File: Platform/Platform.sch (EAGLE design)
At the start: 21 parts, among them IC1 5v

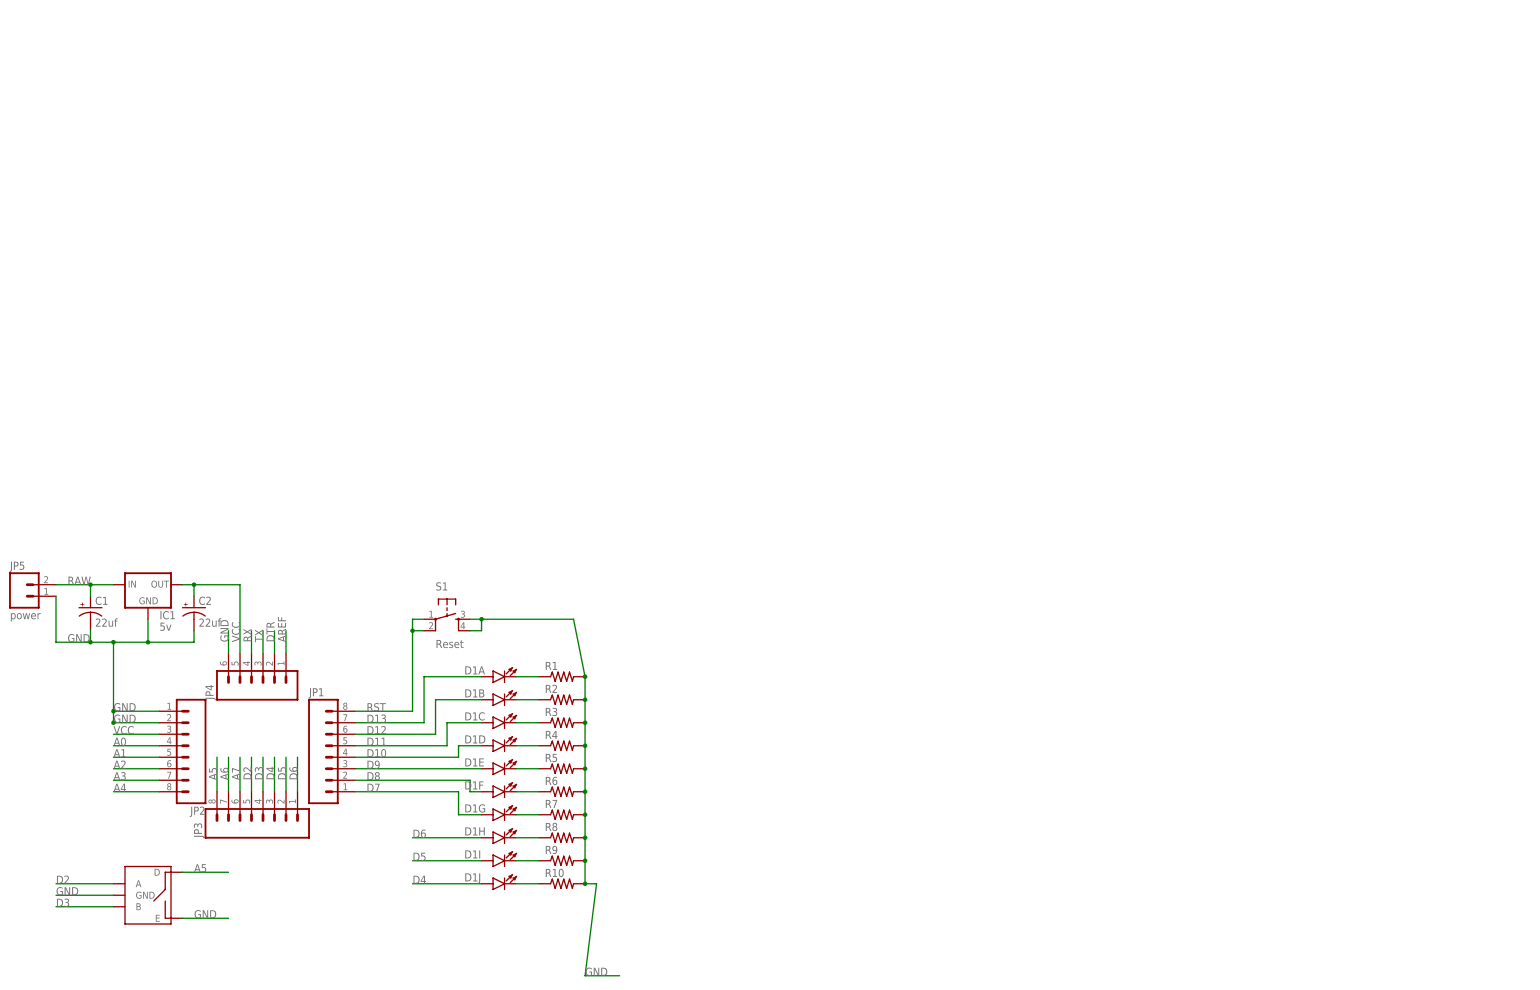
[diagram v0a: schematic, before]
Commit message: fixed up design rules. Copied the actual newest boards into t the project
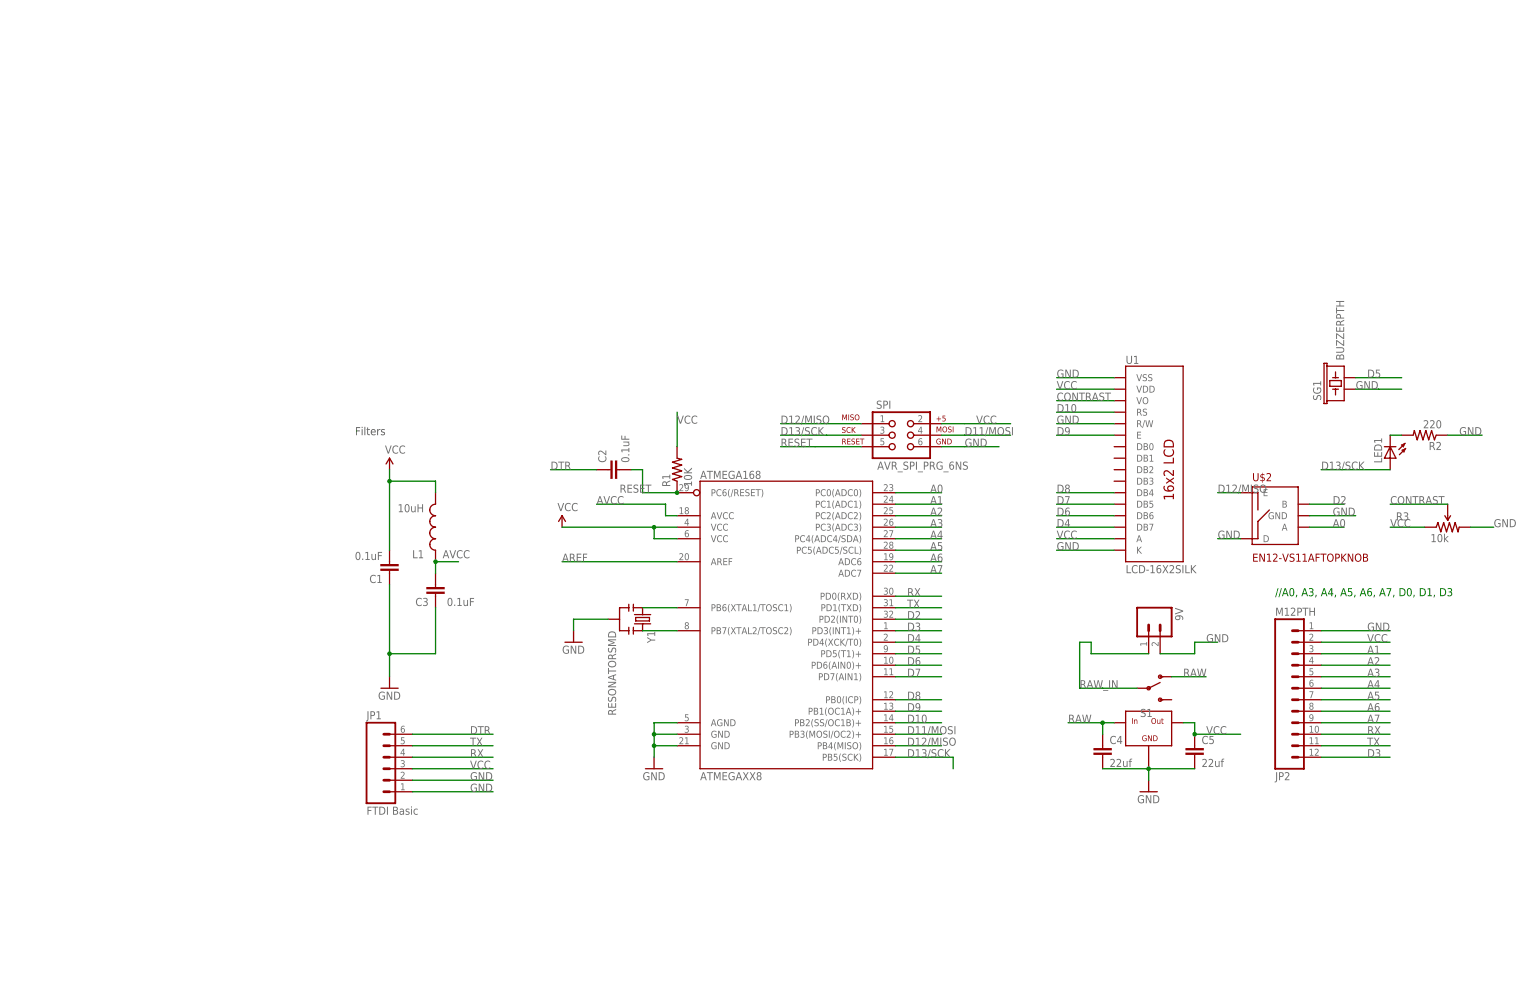
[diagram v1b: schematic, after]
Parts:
- removed D1: (no value), SparkFun:LED_BARGRAPH_10
- removed IC1: 5v, SparkFun:V_REG_78XXSINK
- removed JP3: (no value), SparkFun:M081X08
- removed JP4: (no value), SparkFun:M06SIP
- removed JP5: power, SparkFun:M02PTH
- removed R10, R4, R5, R6, R7, R8, R9: (no value), SparkFun:RESISTOR1206
- removed U$1: EN12-VS11AF, Dustin:EN12-VS11AF
- added 9V: (no value), SparkFun:M02PTH
- added ATMEGAXX8: ATMEGA168, SparkFun:ATMEGA168
- added C3: 0.1uF, SparkFun:CAP0805
- added C4, C5: 22uf, SparkFun:CAP1210
- added L1: 10uH, SparkFun:INDUCTOR0805
- added LED1: (no value), SparkFun:LED3MM
- added SG1: BUZZERPTH, SparkFun:BUZZERPTH
- added SPI: AVR_SPI_PRG_6NS, SparkFun:AVR_SPI_PRG_6NS
- added U$2: EN12-VS11AFTOPKNOB, Dustin:EN12-VS11AFTOPKNOB
- added U1: LCD-16X2SILK, SparkFun:LCD-16X2SILK
- added U3: IFX25001TC, Dustin:IFX25001TC
- added Y1: RESONATORSMD, SparkFun:RESONATORSMD
- C1, C2: value 22uf -> 0.1uF; device SparkFun:CAP_POLPTH2 -> SparkFun:CAP0805
- JP1: value (none) -> FTDI Basic; device SparkFun:M081X08 -> SparkFun:M06SIP
- JP2: value (none) -> M12PTH; device SparkFun:M081X08 -> SparkFun:M12PTH
- R1: value (none) -> 10K; device SparkFun:RESISTOR1206 -> SparkFun:RESISTOR0805-RES
- R2: value (none) -> 220; device SparkFun:RESISTOR1206 -> SparkFun:RESISTOR0805-RES
- R3: value (none) -> 10k; device SparkFun:RESISTOR1206 -> SparkFun:TRIMPOTPTH
- S1: value Reset -> (none); device SparkFun:TAC_SWITCHPTH -> SparkFun:SWITCH-SPSTSMD2
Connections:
- removed net D11: D1C.A, JP1.5
- removed net D12: D1B.A, JP1.6
- removed net D13: D1A.A, JP1.7
- removed net N$10: D1A.C, R1.1
- removed net N$11: D1B.C, R2.1
- removed net N$12: D1C.C, R3.1
- removed net N$13: D1D.C, R4.1
- removed net N$14: D1E.C, R5.1
- removed net N$15: D1F.C, R6.1
- removed net N$16: D1G.C, R7.1
- removed net N$17: D1H.C, R8.1
- removed net N$18: D1I.C, R9.1
- removed net N$19: D1J.C, R10.1
- removed net RST: JP1.8, S1.1, S1.2
- new net AVCC: ATMEGAXX8.AVCC, C3.2, L1.1
- new net CONTRAST: R3.WIPER, U1.VO
- new net D11/MOSI: ATMEGAXX8.PB3(MOSI/OC2)+, SPI.4
- new net D12/MISO: ATMEGAXX8.PB4(MISO), SPI.1, U$2.E
- new net D13/SCK: ATMEGAXX8.PB5(SCK), LED1.A, SPI.3
- new net N$2: LED1.C, R2.2
- new net RAW_IN: 9V.1, S1.P
- new net RESET: ATMEGAXX8.PC6(/RESET), C2.2, R1.1, SPI.5
- new net XTAL1: ATMEGAXX8.PB6(XTAL1/TOSC1), Y1.1
- new net XTAL2: ATMEGAXX8.PB7(XTAL2/TOSC2), Y1.3
- net A0: now also ATMEGAXX8.PC0(ADC0), U$2.A; no longer JP2.4
- net A1: now also ATMEGAXX8.PC1(ADC1), JP2.3; no longer JP2.5
- net A2: now also ATMEGAXX8.PC2(ADC2), JP2.4; no longer JP2.6
- net A3: now also ATMEGAXX8.PC3(ADC3), JP2.5; no longer JP2.7
- net A4: now also ATMEGAXX8.PC4(ADC4/SDA), JP2.6; no longer JP2.8
- net A5: now also ATMEGAXX8.PC5(ADC5/SCL), JP2.7; no longer JP3.8, U$1.D
- net A6: now also ATMEGAXX8.ADC6, JP2.8; no longer JP3.7
- net A7: now also ATMEGAXX8.ADC7, JP2.9; no longer JP3.6
- net AREF: now also ATMEGAXX8.AREF; no longer JP4.1
- net D10: now also ATMEGAXX8.PB2(SS/OC1B)+, U1.RS; no longer D1D.A, JP1.4
- net D2: now also ATMEGAXX8.PD2(INT0), U$2.B; no longer JP3.5, U$1.A
- net D3: now also ATMEGAXX8.PD3(INT1)+, JP2.12; no longer JP3.4, U$1.B
- net D4: now also ATMEGAXX8.PD4(XCK/T0), U1.DB7; no longer D1J.A, JP3.3
- net D5: now also ATMEGAXX8.PD5(T1)+, SG1.2; no longer D1I.A, JP3.2
- net D6: now also ATMEGAXX8.PD6(AIN0)+, U1.DB6; no longer D1H.A, JP3.1
- net D7: now also ATMEGAXX8.PD7(AIN1), U1.DB5; no longer D1G.A, JP1.1
- net D8: now also ATMEGAXX8.PB0(ICP), U1.DB4; no longer D1F.A, JP1.2
- net D9: now also ATMEGAXX8.PB1(OC1A)+, U1.E; no longer D1E.A, JP1.3
- net DTR: now also C2.1, JP1.6; no longer JP4.2
- net GND: now also 9V.2, ATMEGAXX8.AGND, ATMEGAXX8.GND@1, ATMEGAXX8.GND@2, C1.1, C3.1, C4.2, C5.2, JP1.1, JP1.2, R2.1, R3.CW, SG1.1, SPI.6, U$2.D, U$2.GND, U1.K, U1.R/W, U1.VSS, U3.GND, Y1.2; no longer C1.-, C2.-, IC1.GND, JP2.2, JP4.6, JP5.1, R1.2, R10.2, R2.2, R3.2, R4.2, R5.2, R6.2, R7.2, R8.2, R9.2, S1.3, S1.4, U$1.E, U$1.GND
- net RAW: now also C4.1, S1.O, U3.IN; no longer C1.+, IC1.IN, JP5.2
- net RX: now also ATMEGAXX8.PD0(RXD), JP1.4, JP2.10; no longer JP4.4
- net TX: now also ATMEGAXX8.PD1(TXD), JP1.5, JP2.11; no longer JP4.3
- net VCC: now also ATMEGAXX8.VCC@1, ATMEGAXX8.VCC@2, C1.2, C5.1, JP1.3, JP2.2, L1.2, R1.2, R3.CCW, SPI.2, U1.A, U1.VDD, U3.OUT; no longer C2.+, IC1.OUT, JP2.3, JP4.5
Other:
- note added: "//A0, A3, A4, A5, A6, A7, D0, D1, D3"
- note added: "AVR"
- note added: "Filters"
- note added: "Power"
- moved on the sheet: R1, R2

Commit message: added barrel connector and touched up top silk
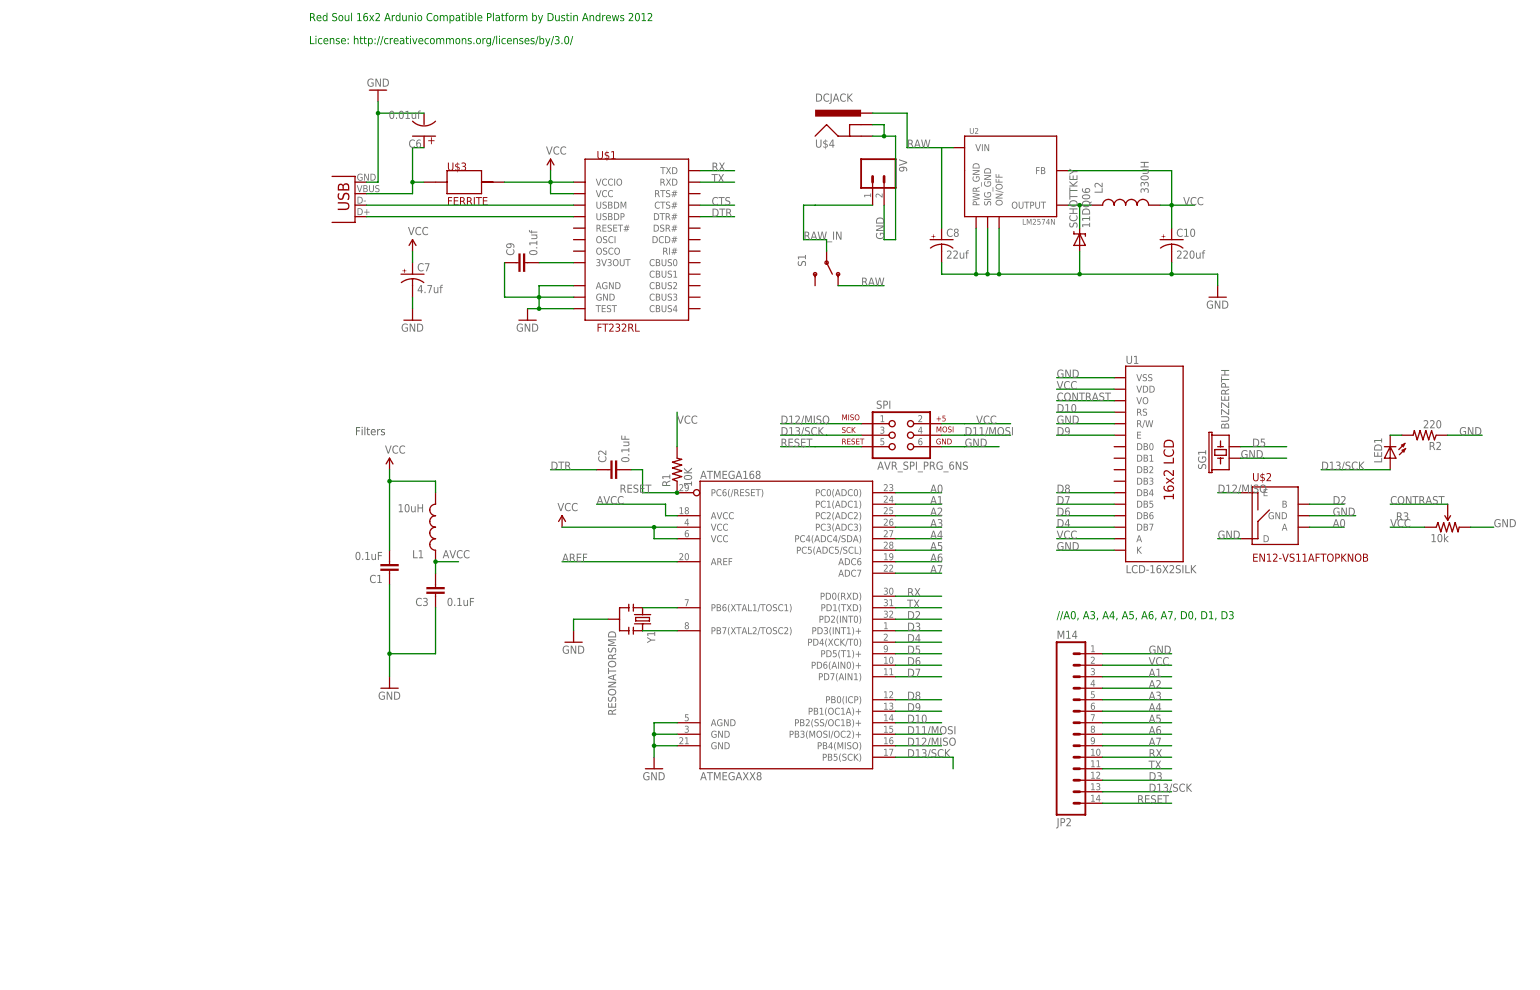
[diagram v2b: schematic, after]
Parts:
- removed C4, C5: 22uf, SparkFun:CAP1210
- removed JP1: FTDI Basic, SparkFun:M06SIP
- removed U3: IFX25001TC, Dustin:IFX25001TC
- added C10: 220uf, SparkFun:CAP_POLPTH1
- added C6: 0.01uf, Dustin:CAP_POL
- added C7: 4.7uf, SparkFun:CAP_POLPTH1
- added C8: 22uf, SparkFun:CAP_POLPTH1
- added C9: 0.1uf, SparkFun:CAP0805
- added L2: 330uH, SparkFun:INDUCTOR1206H*
- added SCHOTTKEY: 11DQ06, SparkFun:DIODE-ZENERPTH
- added U$1: FT232RL, Dustin:FT232RL
- added U$3: FERRITE, Dustin:FERRITE
- added U$4: DCJACK, Dustin:DCJACK
- added U2: LM2574N, Dustin:LM2574N
- added X1: USBSMD, SparkFun:USBSMD
- JP2: value M12PTH -> M14; device SparkFun:M12PTH -> SparkFun:M14
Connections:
- new net CTS: U$1.CTS#
- new net N$1: C6.+, U$3.P$1, X1.VBUS
- new net N$3: L2.1, SCHOTTKEY.C, U2.OUTPUT
- new net N$4: U$1.USBDM, X1.D-
- new net N$5: U$1.USBDP, X1.D+
- new net N$6: C9.2, U$1.3V3OUT
- net D13/SCK: now also JP2.13
- net DTR: now also U$1.DTR#; no longer JP1.6
- net GND: now also C10.-, C6.-, C7.-, C8.-, C9.1, SCHOTTKEY.A, U$1.AGND, U$1.GND, U$1.TEST, U$4.GND, U$4.GNDBREAK, U2.ON/OFF, U2.PWR_GND, U2.SIG_GND, X1.GND; no longer C4.2, C5.2, JP1.1, JP1.2, U3.GND
- net RAW: now also C8.+, U$4.PWR, U2.VIN; no longer C4.1, U3.IN
- net RESET: now also JP2.14
- net RX: now also U$1.TXD; no longer JP1.4
- net TX: now also U$1.RXD; no longer JP1.5
- net VCC: now also C10.+, C7.+, L2.2, U$1.VCC, U$1.VCCIO, U$3.P$2, U2.FB; no longer C5.1, JP1.3, U3.OUT
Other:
- note added: "External Connector for PWR I/O"
- note added: "FTDI"
- note added: "License: http://creativecommons.org/licenses/by/3.0/"
- note added: "On Board Do-Dads"
- note added: "Red Soul 16x2 Ardunio Compatible Platform by Dustin Andrews 2012"
- moved on the sheet: 9V, S1, SG1

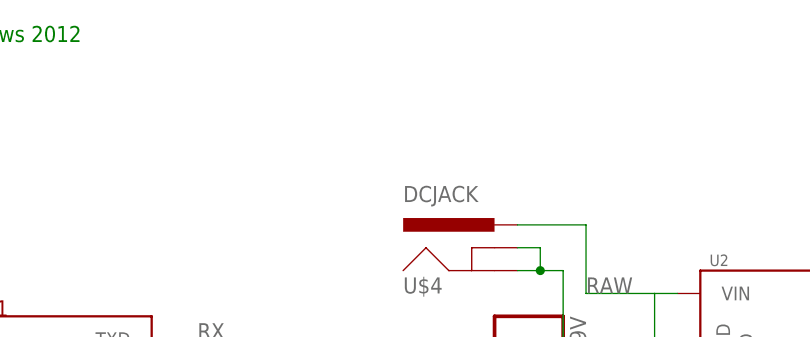
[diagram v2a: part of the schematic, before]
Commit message: updated component locations and traces
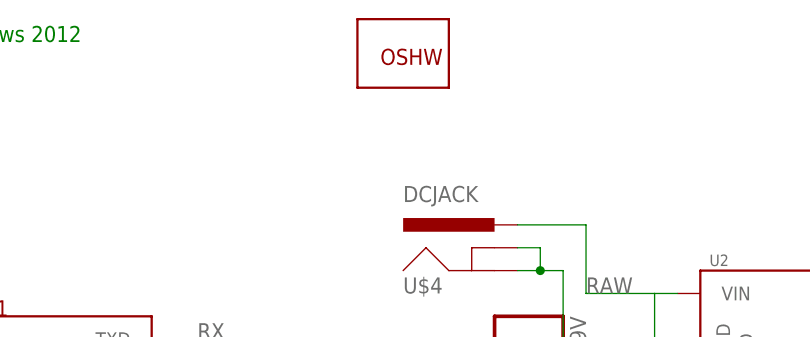
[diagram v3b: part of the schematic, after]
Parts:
- added GOLD_ORB_SM1: OSHWLOGO_GOLD_ORB_SM, NBitWonder:OSHWLOGO_GOLD_ORB_SM
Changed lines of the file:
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@@
 <part name="SCHOTTKEY" library="SparkFun" deviceset="DIODE-ZENER" device="PTH" value="11DQ06"/>
 <part name="U$4" library="Dustin" deviceset="DCJACK" device=""/>
+<part name="GOLD_ORB_SM1" library="NBitWonder" deviceset="OSHWLOGO" device="_GOLD_ORB_SM"/>
 </parts>
 <sheets>
@@
 <instance part="SCHOTTKEY" gate="G$1" x="165.1" y="137.16" rot="R90"/>
 <instance part="U$4" gate="G$1" x="111.76" y="162.56"/>
+<instance part="GOLD_ORB_SM1" gate="G$1" x="101.6" y="180.34"/>
 </instances>
 <busses>
